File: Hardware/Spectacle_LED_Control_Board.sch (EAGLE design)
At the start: 37 parts, among them J1 FTDI_DEVICE, J10 AUDIO-JACK3, J3 USB-MICROB, J4 AUDIO-JACK3, U1 CY8C4146LQI-S422, U2 3.3V/150mA

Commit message: First layout draft
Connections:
- net SERVO_0 renamed LED_0
- net SERVO_1 renamed LED_1
- net SERVO_2 renamed LED_2
- net SERVO_3 renamed LED_3
- net SERVO_4 renamed LED_4
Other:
- note added: "LED Connectors"
- note removed: "Servos"
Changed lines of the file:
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@@
 <?xml version="1.0" encoding="utf-8"?>
 <!DOCTYPE eagle SYSTEM "eagle.dtd">
-<eagle version="7.5.0">
+<eagle version="7.6.0">
 <drawing>
 <settings>
@@
 <grid distance="0.1" unitdist="inch" unit="inch" style="lines" multiple="1" display="no" altdistance="0.01" altunitdist="inch" altunit="inch"/>
 <layers>
-<layer number="1" name="Top" color="4" fill="1" visible="yes" active="no"/>
-<layer number="2" name="Route2" color="1" fill="3" visible="yes" active="no"/>
-<layer number="3" name="Route3" color="4" fill="3" visible="yes" active="no"/>
-<layer number="4" name="Route4" color="1" fill="4" visible="yes" active="no"/>
-<layer number="5" name="Route5" color="4" fill="4" visible="yes" active="no"/>
-<layer number="6" name="Route6" color="1" fill="8" visible="yes" active="no"/>
-<layer number="7" name="Route7" color="4" fill="8" visible="yes" active="no"/>
-<layer number="8" name="Route8" color="1" fill="2" visible="yes" active="no"/>
-<layer number="9" name="Route9" color="4" fill="2" visible="yes" active="no"/>
-<layer number="10" name="Route10" color="1" fill="7" visible="yes" active="no"/>
-<layer number="11" name="Route11" color="4" fill="7" visible="yes" active="no"/>
-<layer number="12" name="Route12" color="1" fill="5" visible="yes" active="no"/>
-<layer number="13" name="Route13" color="4" fill="5" visible="yes" active="no"/>
-<layer number="14" name="Route14" color="1" fill="6" visible="yes" active="no"/>
-<layer number="15" name="Route15" color="4" fill="6" visible="yes" active="no"/>
-<layer number="16" name="Bottom" color="1" fill="1" visible="yes" active="no"/>
-<layer number="17" name="Pads" color="2" fill="1" visible="yes" active="no"/>
-<layer number="18" name="Vias" color="2" fill="1" visible="yes" active="no"/>
-<layer number="19" name="Unrouted" color="6" fill="1" visible="yes" active="no"/>
-<layer number="20" name="Dimension" color="15" fill="1" visible="yes" active="no"/>
-<layer number="21" name="tPlace" color="16" fill="1" visible="yes" active="no"/>
-<layer number="22" name="bPlace" color="14" fill="1" visible="yes" active="no"/>
-<layer number="23" name="tOrigins" color="15" fill="1" visible="yes" active="no"/>
-<layer number="24" name="bOrigins" color="15" fill="1" visible="yes" active="no"/>
-<layer number="25" name="tNames" color="7" fill="1" visible="yes" active="no"/>
-<layer number="26" name="bNames" color="7" fill="1" visible="yes" active="no"/>
-<layer number="27" name="tValues" color="7" fill="1" visible="yes" active="no"/>
-<layer number="28" name="bValues" color="7" fill="1" visible="yes" active="no"/>
+<layer number="1" name="Top" color="4" fill="1" visible="no" active="no"/>
+<layer number="2" name="Route2" color="1" fill="3" visible="no" active="no"/>
+<layer number="3" name="Route3" color="4" fill="3" visible="no" active="no"/>
+<layer number="4" name="Route4" color="1" fill="4" visible="no" active="no"/>
+<layer number="5" name="Route5" color="4" fill="4" visible="no" active="no"/>
+<layer number="6" name="Route6" color="1" fill="8" visible="no" active="no"/>
+<layer number="7" name="Route7" color="4" fill="8" visible="no" active="no"/>
+<layer number="8" name="Route8" color="1" fill="2" visible="no" active="no"/>
+<layer number="9" name="Route9" color="4" fill="2" visible="no" active="no"/>
+<layer number="10" name="Route10" color="1" fill="7" visible="no" active="no"/>
+<layer number="11" name="Route11" color="4" fill="7" visible="no" active="no"/>
+<layer number="12" name="Route12" color="1" fill="5" visible="no" active="no"/>
+<layer number="13" name="Route13" color="4" fill="5" visible="no" active="no"/>
+<layer number="14" name="Route14" color="1" fill="6" visible="no" active="no"/>
+<layer number="15" name="Route15" color="4" fill="6" visible="no" active="no"/>
+<layer number="16" name="Bottom" color="1" fill="1" visible="no" active="no"/>
+<layer number="17" name="Pads" color="2" fill="1" visible="no" active="no"/>
+<layer number="18" name="Vias" color="2" fill="1" visible="no" active="no"/>
+<layer number="19" name="Unrouted" color="6" fill="1" visible="no" active="no"/>
+<layer number="20" name="Dimension" color="15" fill="1" visible="no" active="no"/>
+<layer number="21" name="tPlace" color="16" fill="1" visible="no" active="no"/>
+<layer number="22" name="bPlace" color="14" fill="1" visible="no" active="no"/>
+<layer number="23" name="tOrigins" color="15" fill="1" visible="no" active="no"/>
+<layer number="24" name="bOrigins" color="15" fill="1" visible="no" active="no"/>
+<layer number="25" name="tNames" color="7" fill="1" visible="no" active="no"/>
+<layer number="26" name="bNames" color="7" fill="1" visible="no" active="no"/>
+<layer number="27" name="tValues" color="7" fill="1" visible="no" active="no"/>
+<layer number="28" name="bValues" color="7" fill="1" visible="no" active="no"/>
 <layer number="29" name="tStop" color="7" fill="3" visible="no" active="no"/>
 <layer number="30" name="bStop" color="7" fill="6" visible="no" active="no"/>
@@
 <layer number="35" name="tGlue" color="7" fill="4" visible="no" active="no"/>
 <layer number="36" name="bGlue" color="7" fill="5" visible="no" active="no"/>
-<layer number="37" name="tTest" color="7" fill="1" visible="yes" active="no"/>
-<layer number="38" name="bTest" color="7" fill="1" visible="yes" active="no"/>
+<layer number="37" name="tTest" color="7" fill="1" visible="no" active="no"/>
+<layer number="38" name="bTest" color="7" fill="1" visible="no" active="no"/>
 <layer number="39" name="tKeepout" color="4" fill="11" visible="no" active="no"/>
 <layer number="40" name="bKeepout" color="1" fill="11" visible="no" active="no"/>
@@
 <layer number="44" name="Drills" color="7" fill="1" visible="no" active="no"/>
 <layer number="45" name="Holes" color="7" fill="1" visible="no" active="no"/>
-<layer number="46" name="Milling" color="3" fill="1" visible="yes" active="no"/>
-<layer number="47" name="Measures" color="7" fill="1" visible="yes" active="no"/>
-<layer number="48" name="Document" color="7" fill="1" visible="yes" active="no"/>
-<layer number="49" name="Reference" color="7" fill="1" visible="yes" active="no"/>
-<layer number="50" name="dxf" color="7" fill="1" visible="yes" active="no"/>
-<layer number="51" name="tDocu" color="6" fill="1" visible="yes" active="no"/>
-<layer number="52" name="bDocu" color="7" fill="1" visible="yes" active="no"/>
-<layer number="53" name="tGND_GNDA" color="7" fill="9" visible="yes" active="no"/>
-<layer number="54" name="bGND_GNDA" color="1" fill="9" visible="yes" active="no"/>
-<layer number="56" name="wert" color="7" fill="1" visible="yes" active="no"/>
-<layer number="57" name="tCAD" color="7" fill="1" visible="yes" active="no"/>
-<layer number="59" name="tCarbon" color="7" fill="1" visible="yes" active="no"/>
-<layer number="60" name="bCarbon" color="7" fill="1" visible="yes" active="no"/>
+<layer number="46" name="Milling" color="3" fill="1" visible="no" active="no"/>
+<layer number="47" name="Measures" color="7" fill="1" visible="no" active="no"/>
+<layer number="48" name="Document" color="7" fill="1" visible="no" active="no"/>
+<layer number="49" name="Reference" color="7" fill="1" visible="no" active="no"/>
+<layer number="50" name="dxf" color="7" fill="1" visible="no" active="no"/>
+<layer number="51" name="tDocu" color="6" fill="1" visible="no" active="no"/>
+<layer number="52" name="bDocu" color="7" fill="1" visible="no" active="no"/>
+<layer number="53" name="tGND_GNDA" color="7" fill="9" visible="no" active="no"/>
+<layer number="54" name="bGND_GNDA" color="1" fill="9" visible="no" active="no"/>
+<layer number="56" name="wert" color="7" fill="1" visible="no" active="no"/>
+<layer number="57" name="tCAD" color="7" fill="1" visible="no" active="no"/>
+<layer number="59" name="tCarbon" color="7" fill="1" visible="no" active="no"/>
+<layer number="60" name="bCarbon" color="7" fill="1" visible="no" active="no"/>
 <layer number="90" name="Modules" color="5" fill="1" visible="yes" active="yes"/>
 <layer number="91" name="Nets" color="2" fill="1" visible="yes" active="yes"/>
@@
 <text x="147.32" y="114.3" size="3.81" layer="97" font="vector">MCU</text>
 <text x="149.86" y="106.68" size="3.81" layer="97" font="vector">Connectors</text>
-<text x="124.46" y="81.28" size="3.81" layer="97" font="vector">Servos</text>
+<text x="114.3" y="76.2" size="3.81" layer="97" font="vector">LED
+Connectors</text>
 <text x="81.28" y="88.9" size="3.81" layer="97" font="vector">Power
 Supply</text>
@@
 </segment>
 </net>
-<net name="SERVO_0" class="0">
+<net name="LED_0" class="0">
 <segment>
 <pinref part="U1" gate="G3" pin="P3.0"/>
@@
 </segment>
 </net>
-<net name="SERVO_1" class="0">
+<net name="LED_1" class="0">
 <segment>
 <pinref part="U1" gate="G3" pin="P2.6"/>
@@
 </segment>
 </net>
-<net name="SERVO_2" class="0">
+<net name="LED_2" class="0">
 <segment>
 <pinref part="U1" gate="G0" pin="P1.0"/>
@@
 </segment>
 </net>
-<net name="SERVO_3" class="0">
+<net name="LED_3" class="0">
 <segment>
 <pinref part="U1" gate="G0" pin="P1.2"/>
@@
 </segment>
 </net>
-<net name="SERVO_4" class="0">
+<net name="LED_4" class="0">
 <segment>
 <pinref part="U1" gate="G3" pin="P2.0"/>

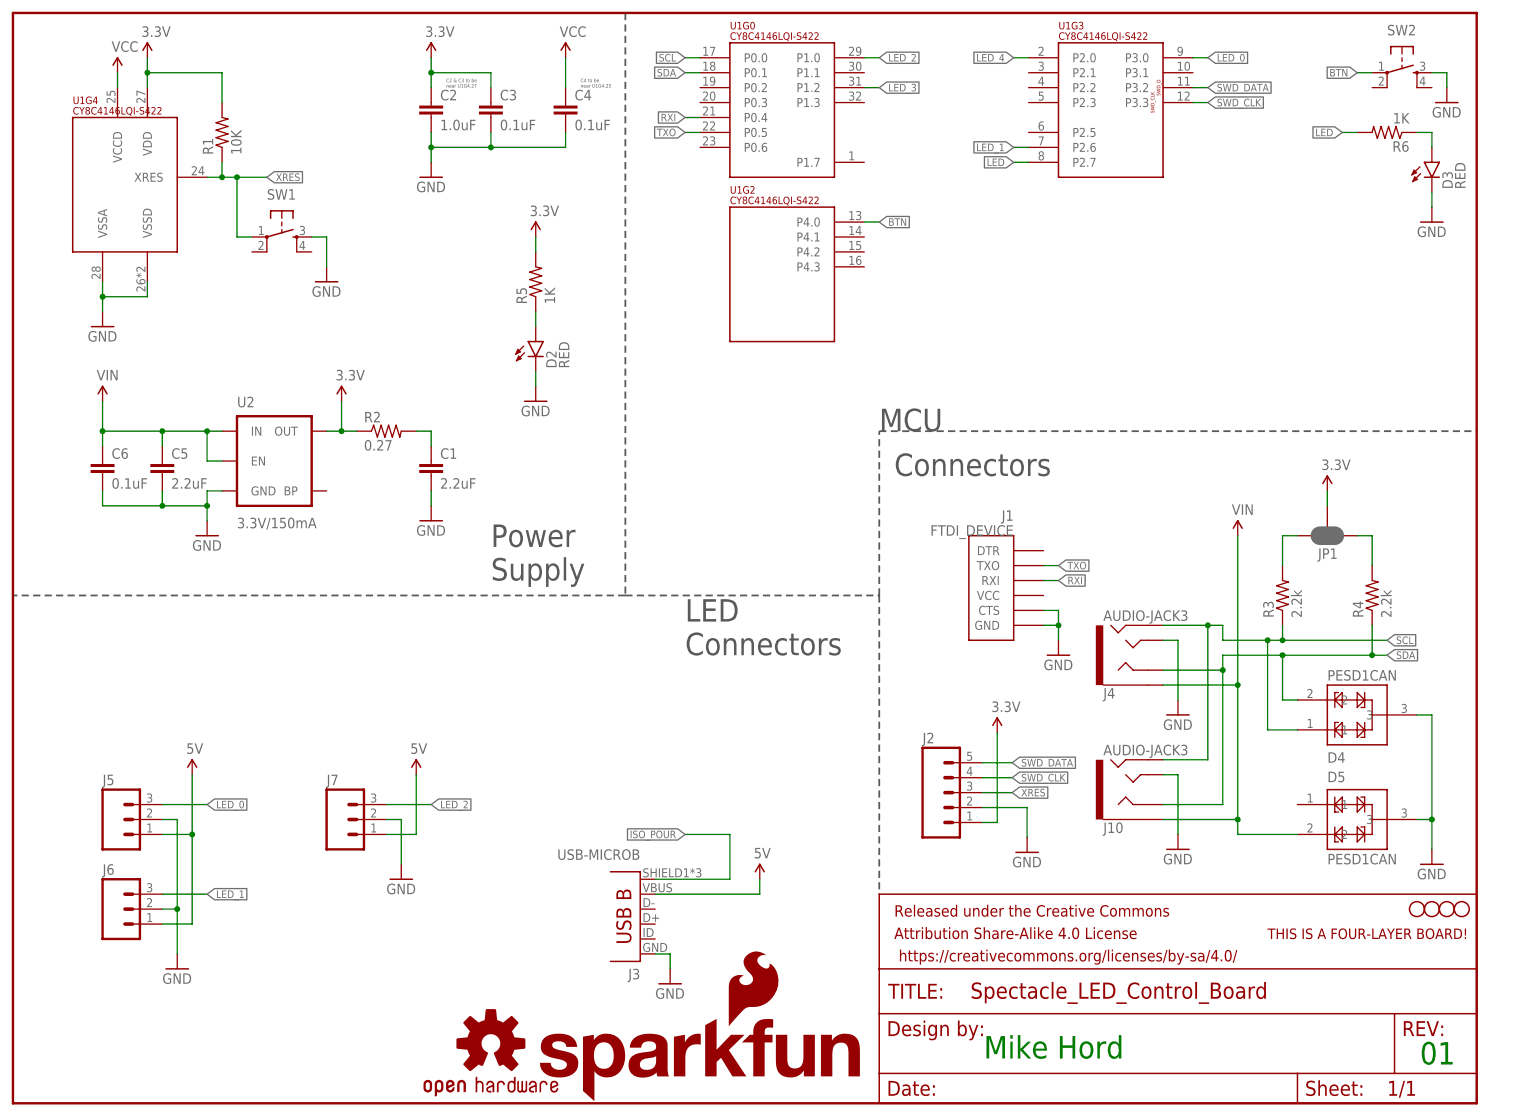
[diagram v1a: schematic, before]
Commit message: Add spectacle logo silk
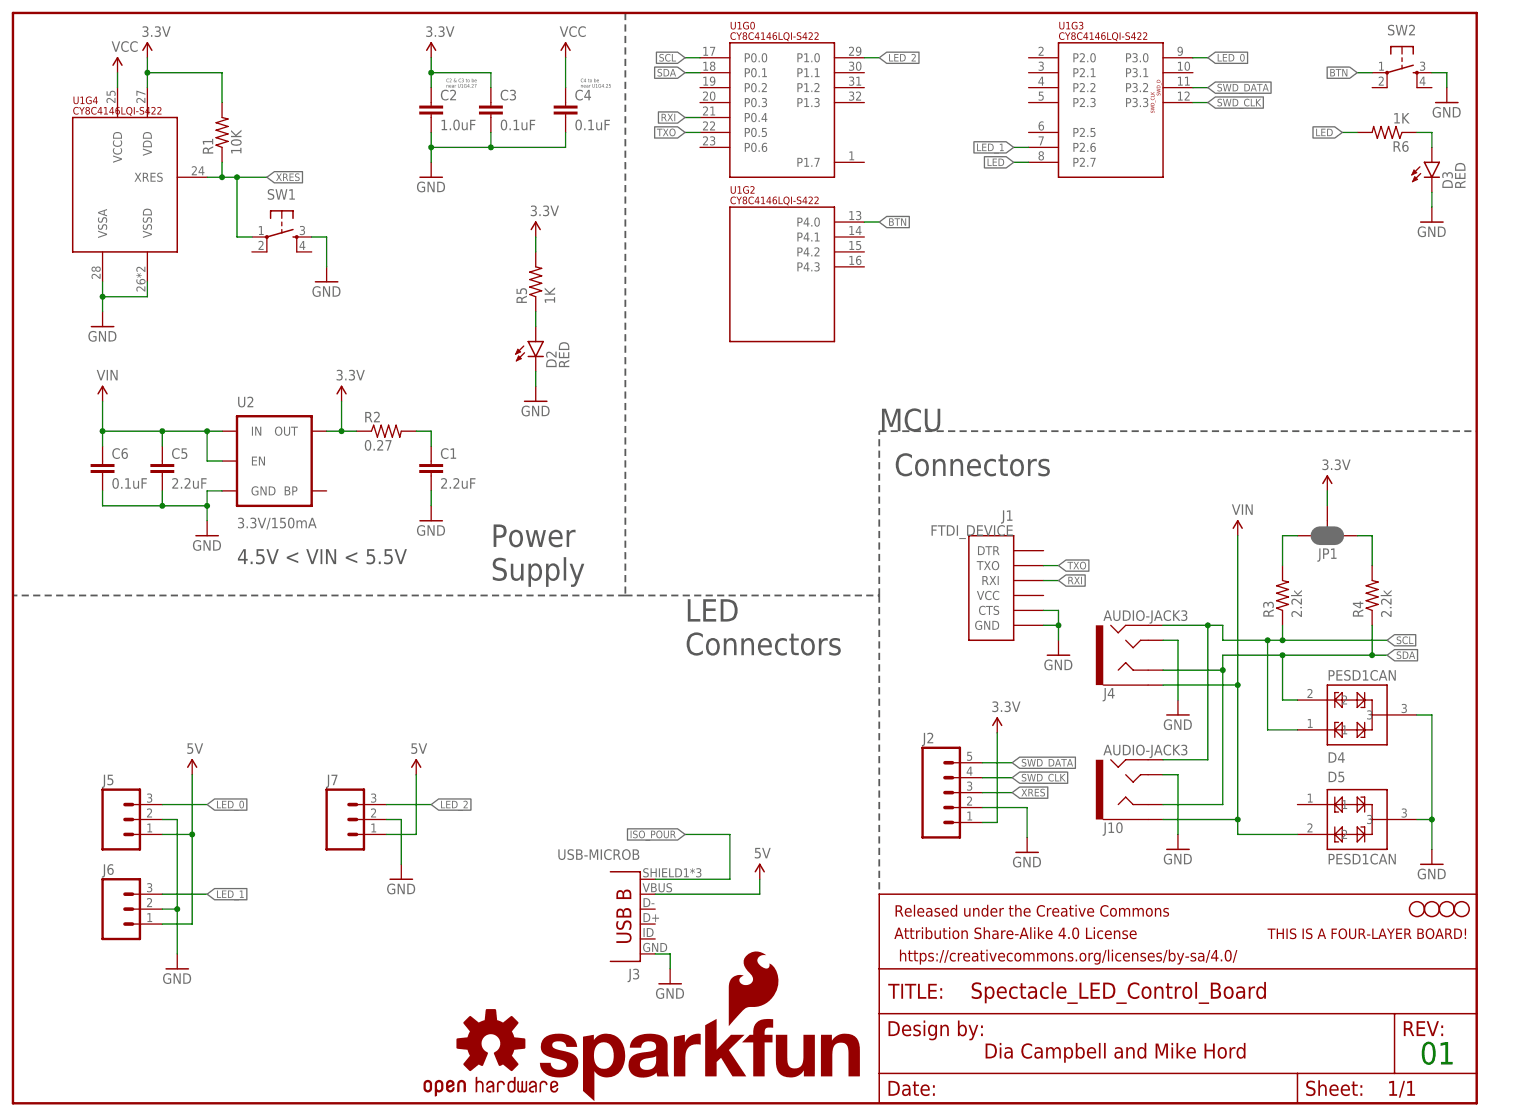
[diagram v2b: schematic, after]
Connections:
- removed net LED_3: U1G0.P1.2
- removed net LED_4: U1G3.P2.0
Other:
- note added: "4.5V < VIN < 5.5V"
- note added: "Dia Campbell and Mike Hord"
- note removed: "Mike Hord"
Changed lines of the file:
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@@
 <layer number="255" name="routoute" color="7" fill="1" visible="yes" active="yes"/>
 </layers>
-<schematic xreflabel="%F%N/%S" xrefpart="/%S.%C%R">
+<schematic xreflabel="%F%N/%S" xrefpart="1_/%S.%C%R">
 <attributes>
 </attributes>
@@
 <wire x1="104.14" y1="86.36" x2="147.32" y2="86.36" width="0.3048" layer="97" style="longdash"/>
 <wire x1="147.32" y1="86.36" x2="147.32" y2="35.56" width="0.3048" layer="97" style="longdash"/>
-<text x="165.1" y="7.62" size="3.81" layer="91" font="vector">Mike Hord</text>
+<text x="165.1" y="7.62" size="2.54" layer="94" font="vector">Dia Campbell and Mike Hord</text>
 <text x="239.268" y="6.604" size="3.81" layer="91" font="vector">01</text>
 <wire x1="147.32" y1="86.36" x2="147.32" y2="114.3" width="0.3048" layer="97" style="longdash"/>
@@
 <text x="81.28" y="88.9" size="3.81" layer="97" font="vector">Power
 Supply</text>
+<text x="38.1" y="91.694" size="2.54" layer="97" font="vector">4.5V &lt; VIN &lt; 5.5V</text>
 </plain>
 <instances>
@@
 </segment>
 </net>
-<net name="LED_3" class="0">
-<segment>
-<pinref part="U1" gate="G0" pin="P1.2"/>
-<wire x1="144.78" y1="172.72" x2="147.32" y2="172.72" width="0.1524" layer="91"/>
-<label x="147.32" y="172.72" size="1.27" layer="95" xref="yes"/>
-</segment>
-</net>
-<net name="LED_4" class="0">
-<segment>
-<pinref part="U1" gate="G3" pin="P2.0"/>
-<wire x1="172.72" y1="177.8" x2="170.18" y2="177.8" width="0.1524" layer="91"/>
-<label x="170.18" y="177.8" size="1.27" layer="95" rot="R180" xref="yes"/>
-</segment>
-</net>

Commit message: review edit list
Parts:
- added FD1, FD2: FIDUCIALUFIDUCIAL, SparkFun-Aesthetics:FIDUCIALUFIDUCIAL
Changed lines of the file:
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@@
 <?xml version="1.0" encoding="utf-8"?>
 <!DOCTYPE eagle SYSTEM "eagle.dtd">
-<eagle version="7.6.0">
+<eagle version="7.3.0">
 <drawing>
 <settings>
@@
 <layer number="255" name="routoute" color="7" fill="1" visible="yes" active="yes"/>
 </layers>
-<schematic xreflabel="%F%N/%S" xrefpart="1_/%S.%C%R">
+<schematic xreflabel="%F%N/%S" xrefpart="/%S.%C%R">
 <attributes>
 </attributes>
@@
 <part name="GND16" library="SparkFun-Aesthetics" deviceset="GND" device=""/>
 <part name="GND17" library="SparkFun-Aesthetics" deviceset="GND" device=""/>
+<part name="FD1" library="SparkFun-Aesthetics" deviceset="FIDUCIAL" device="UFIDUCIAL"/>
+<part name="FD2" library="SparkFun-Aesthetics" deviceset="FIDUCIAL" device="UFIDUCIAL"/>
 </parts>
 <sheets>
@@
 <text x="81.28" y="88.9" size="3.81" layer="97" font="vector">Power
 Supply</text>
-<text x="38.1" y="91.694" size="2.54" layer="97" font="vector">4.5V &lt; VIN &lt; 5.5V</text>
+<text x="4.318" y="88.9" size="2.54" layer="97" font="vector">4.5V &lt; VIN &lt; 5.5V</text>
 </plain>
 <instances>
@@
 <instance part="GND16" gate="1" x="198.12" y="43.18"/>
 <instance part="GND17" gate="1" x="27.94" y="22.86"/>
+<instance part="FD1" gate="G$1" x="238.76" y="25.4"/>
+<instance part="FD2" gate="G$1" x="243.84" y="25.4"/>
 </instances>
 <busses>
